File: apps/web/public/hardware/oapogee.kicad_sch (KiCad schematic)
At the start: 37 parts, among them J1 USB-C-16P, J2 S2B-PH-K-S, J3 ANT-902-928, J4 SWD-PADS, SW1 ARM-SWITCH, SW2 BOOT-BUTTON, SW3 RESET-BUTTON, U1 MCP73831, U2 TPS63001, U3 RP2350A, U4 W25Q128JVSIQ, U5 BMP390, U6 ICM-42688-P, U7 ADXL375, U8 SX1262, U9 MAX-M10S

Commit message: Replace the addressable LED, and catch the export lying about it
The status LED is three plain dice in one package now, driven by three pins
through three resistors, rather than an addressable part on one. The reason is
in the bill of materials: the WS2812 family wants a supply above the only rail
this board has, and a part run under its minimum works for whoever tested it and
does something else cold. One resistor per colour because the three dice do not
share a forward voltage, so a single shared one gives three brightnesses and no
way to fix one without moving the others.

Doing it exposed something worse than the LED.

Renaming three pins on the microcontroller left a stale entry in its schematic
pin arrangement, which still named the old label. tscircuit could not resolve
it, and the whole chip failed to create. The export printed success and exited
zero. The netlist came out with 64 of its 123 traces, missing every connection
that touches the microcontroller, and check-pcb reported a clean board: nothing
was unrouted, because the traces that would have been unrouted no longer
existed. I nearly committed a fabrication package for a board with no
microcontroller connected to anything.

Two checks now stand in front of that. Source errors are read before anything
else, because a netlist missing half its connections is not a board with a
routing problem, it is not the board. And the number of traces declared in the
circuit source is compared against the number that reached the netlist, since a
selector that resolves to nothing removes a connection without removing a line
of source, which is invisible to every other measurement. Both are blockers.

The board is 35 components, 119 routed traces, 195 vias, nothing missing,
nothing unconnected, no placement errors, fabrication package regenerated.
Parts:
- removed D1: RGB-LED, symbol Device:U_RGB-LED
- removed GND (x4): GND, symbol Custom:rail_down
- added D1: RGB-LED-CC, symbol Device:U_RGB-LED-CC
- added GND (x3): GND, symbol Custom:rail_down
- added R10: 330Ω, symbol Device:boxresistor_right
- added R11, R12: 220Ω, symbol Device:boxresistor_right
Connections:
- net GND: now also J4.3 (GND), D1.4 (K)
- net at SW1.2 (B): now also LS1.2 (GND); no longer J4.3 (GND)
- net U3_LED renamed U3_LED_R
- net U3_LED_R: now also R10.1
- new net: D1.2 (A_G), R11.2
- new net: D1.1 (A_R), R10.2
- new net D1_A_B: D1.3 (A_B), R12.2
- new net U3_LED_B: R12.1, U3.13 (LED_B)
- new net U3_LED_G: R11.1, U3.16 (LED_G)

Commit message: Choose the remaining parts, and fix what the datasheets said was wrong
The bill of materials had eleven rows with no part behind them, which meant
the design was not actually finished: several of those rows decide how the
board behaves rather than just what it costs. Reading the datasheets to close
them turned up two things the schematic had wrong.

The buck-boost's output capacitor was 10 uF. SLVS520C section 8.2.2.3.2 asks
for a nominal 15 uF, and a small ceramic delivers well under its marked value
under DC bias, so the rail was short of the datasheet twice over. C1 and C2
were one BOM line and are now two, because the datasheet asks for two values:
at least 4.7 uF in, 15 uF nominal out. C2 is 22 uF to leave room for derating.

The status LED was described as common anode in the BOM and wired as common
cathode on the schematic. The schematic was right.

Parts now chosen, each with the datasheet facts that chose them:

  LS1  Murata PKLCS1212E4001-R1, piezo rather than magnetic. A piezo element
       is capacitive, so a pin drives it directly; a magnetic buzzer is a coil
       and would have brought a transistor and a flyback diode with it.
  SW1  C&K JS102011SCQN, SPDT with one throw wired. Driving the spare throw
       would give a defined level in both positions, but the wiper is open
       mid-throw, so the pin would float on every actuation.
  J1   GCT USB4085-GF-A, through hole. The USB connector is the only part of
       a flight computer a person yanks on, and surface mount pads tear off.
  J3   Hirose U.FL-R-SMT-1(10). A socket, because the radiator is still an
       open measurement and soldering it down would close the question by
       making it too annoying to ask. Thirty mating cycles: fit it once.
  SW2  Omron B3U-1000P for boot and reset. 153 gf is stiff on purpose.
  SW3
  L2   Coilcraft LPS3015 or another series from SLVS520C Table 2. At 2.5 MHz
       the core material decides efficiency, so the datasheet's own list is
       the selectio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
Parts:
- removed GND (x3): GND, symbol Custom:rail_down
- removed J1: USB-C-16P, symbol Device:U_USB-C-16P
- removed J3: ANT-902-928, symbol Device:U_ANT-902-928
- removed LS1: PIEZO-BUZZER, symbol Device:U_PIEZO-BUZZER
- removed SW1: ARM-SWITCH, symbol Device:U_ARM-SWITCH
- removed SW2: BOOT-BUTTON, symbol Device:U_BOOT-BUTTON
- removed SW3: RESET-BUTTON, symbol Device:U_RESET-BUTTON
- added GND (x3): GND, symbol Custom:rail_down
- added J1: USB4085-GF-A, symbol Device:U_USB4085-GF-A
- added J3: U.FL-R-SMT-1(10), symbol Device:U_U.FL-R-SMT-1(10)
- added LS1: PKLCS1212E4001-R1, symbol Device:U_PKLCS1212E4001-R1
- added SW1: JS102011SCQN, symbol Device:U_JS102011SCQN
- added SW2, SW3: B3U-1000P, symbol Device:U_B3U-1000P
- C2: value 10uF -> 22uF
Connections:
- net GND: now also J1.2 (GND), SW2.3 (B1), SW2.4 (B2), SW3.3 (B1), SW3.4 (B2)
- net J1_CC2: now also J1.6 (CC2)
- net U3_ARM: now also SW1.1 (A)
- net U3_BUZZER: now also LS1.1 (IN)
- net U3_QSPI_CS: now also SW2.1 (A1), SW2.2 (A2)
- net U3_RUN: now also SW3.2 (A2)
- net U3_USB_DM: now also J1.4 (DM)
- net U3_USB_DP: now also J1.3 (DP)
- net U8_ANT: now also J3.1 (ANT)
- net at U1.4 (VDD): now also J1.1 (VBUS)
- net at R1.1: now also J1.5 (CC1)
- net at U9.2 (GND): now also J3.2 (GND)
- new net: LS1.2 (GND), SW1.2 (B)

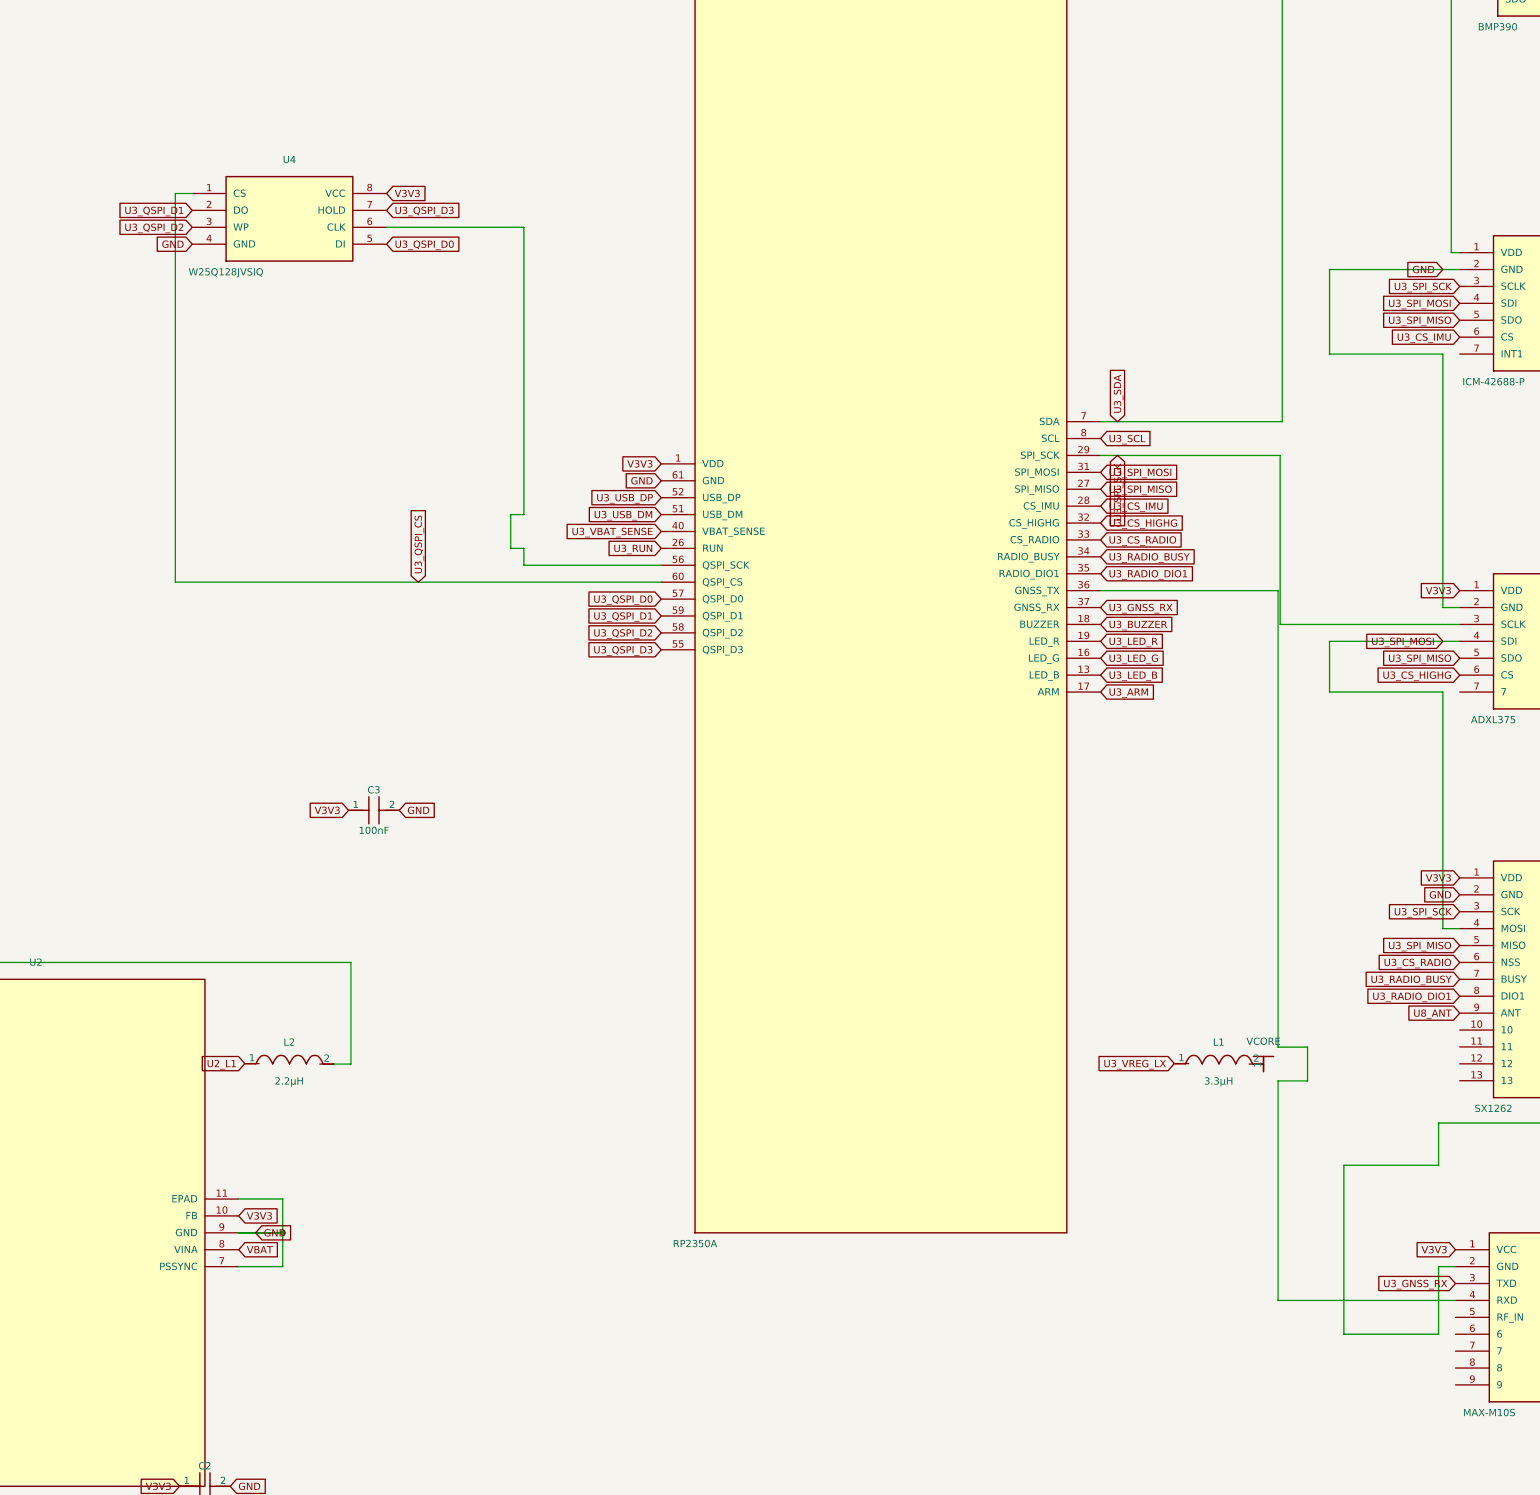
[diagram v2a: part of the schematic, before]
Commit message: Add the crystal, without which the board cannot be flashed
XIN and XOUT were declared on the RP2350 and connected to nothing. That is not
a missing refinement, it is a dead board: "Hardware design with RP2350" chapter
4 says the internal oscillator's frequency is not well defined or controlled,
varying by chip, supply and temperature, and that applications relying on exact
frequencies are not possible without an external source, naming USB as the
example. USB is the only connector this board has and drag-and-drop UF2 loading
is why this microcontroller family was chosen at all.

Every value is Raspberry Pi's. Y1 is the ABM8-272-T3 they specify and the Pico 2
uses. C4 and C5 are 15 pF, which in series is 7.5 pF, plus the 3 pF of track and
pin parasitic capacitance the guide tells you to assume, reaching 10.5 pF
against the crystal's 10 pF load. R13 is the 1k that stops a 50 ohm ESR crystal
being overdriven at 3.3 V IOVDD. The load capacitors are C0G rather than the
X5R used elsewhere, because a payload sits in the sun and then climbs into cold
air, and a load capacitance that drifts detunes the oscillator.

The board is 39 components and 128 routed traces, still with no fabrication
blockers. The build page now solders the crystal as a fact rather than "if the
design uses one", and fits the arming switch, which neither path did.

Also, the ground station page said each packet carries the payload's device
identifier. It does not. The header is eight bytes of version, type, sequence,
state and timestamp, and there is no identifier anywhere in it. The identity
exists but is written to the flight log, so it tells you whose flight it was
afterwards and not at the time. The page now says that, says what to do instead
(agree different frequencies), and the question of whether an identifier belongs
in the header is written up in open-questions with the airtime cost stated
rather than settled quietly.

Checkpoint 8 sent the reader to a stability margin range on the safety page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
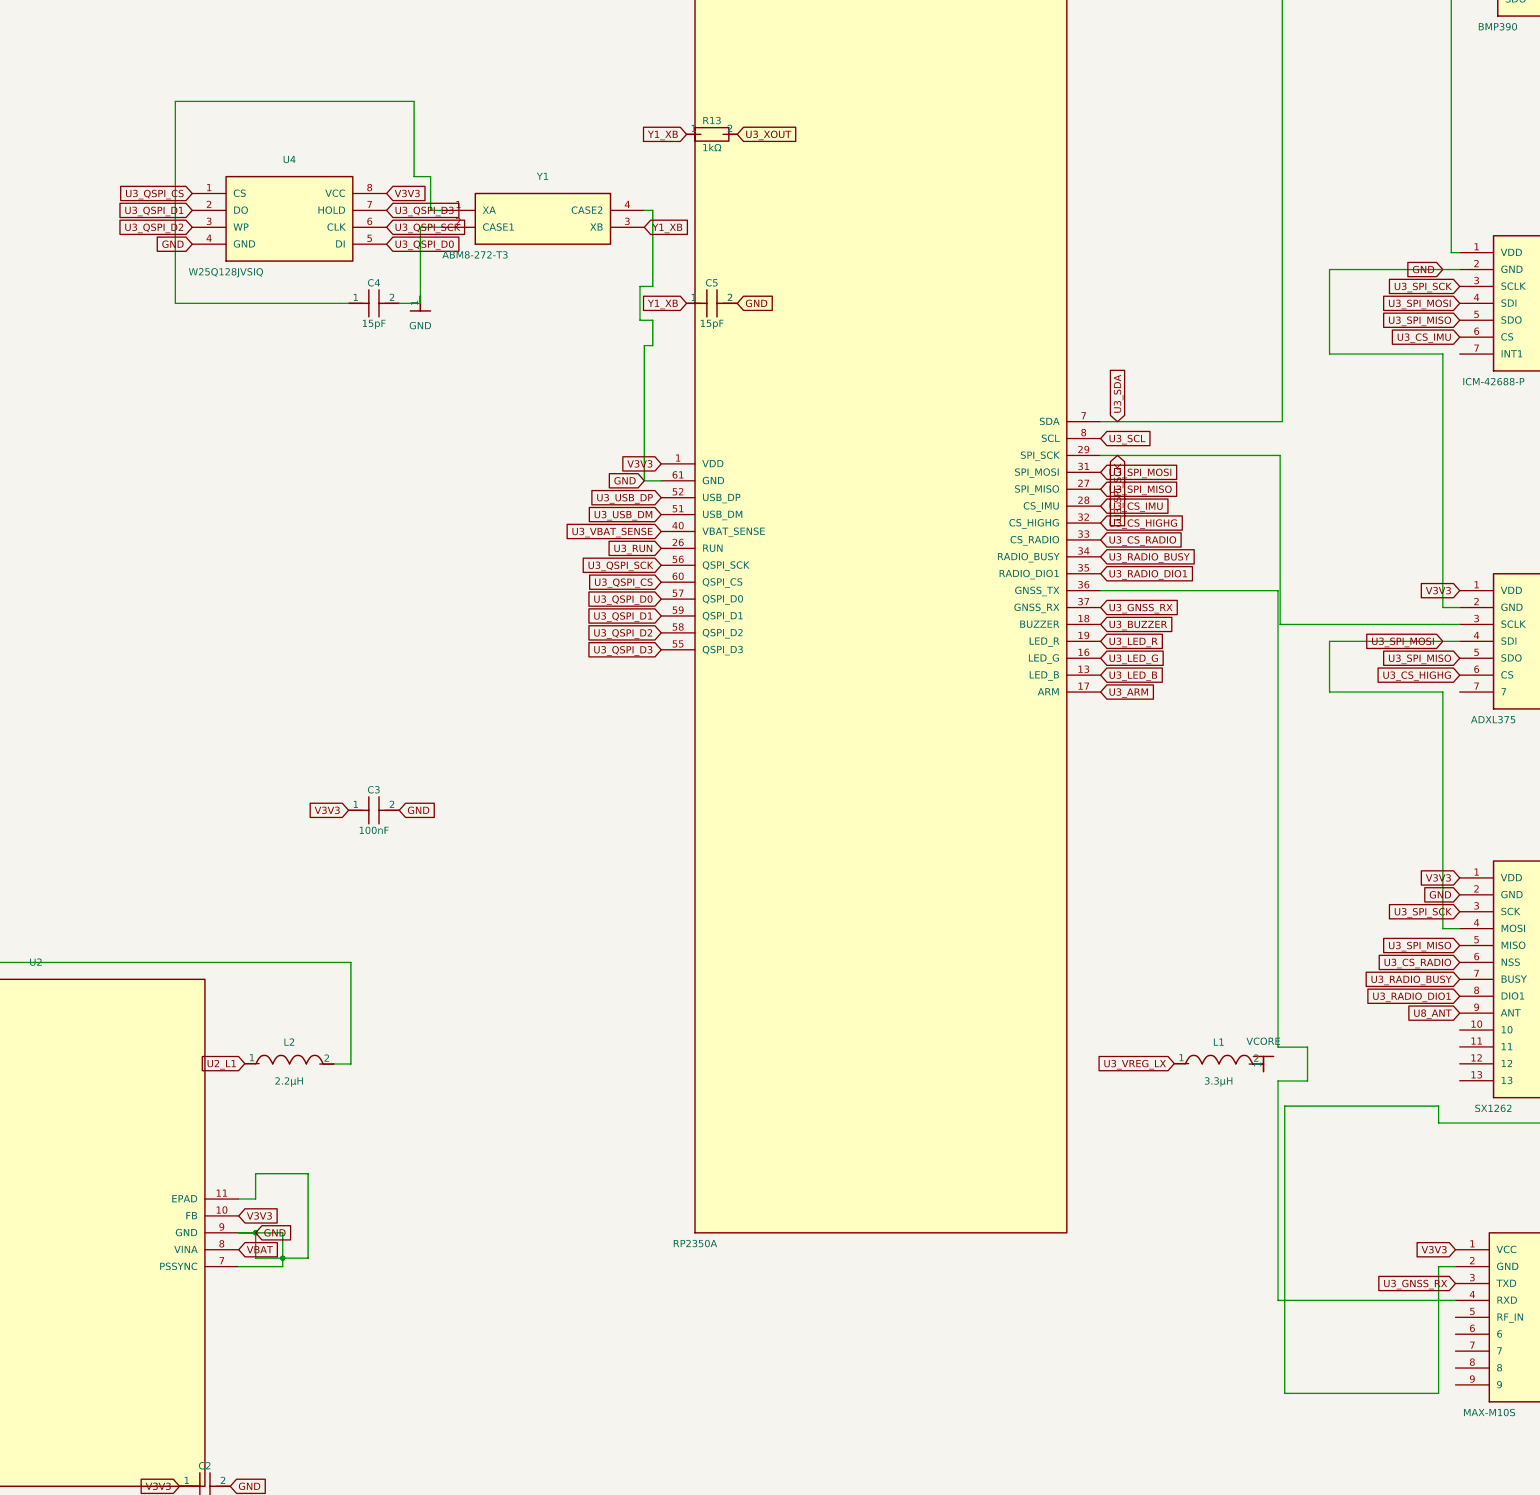
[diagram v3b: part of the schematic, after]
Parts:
- removed GND (x3): GND, symbol Custom:rail_down
- added C4, C5: 15pF, symbol Device:capacitor_right
- added GND (x4): GND, symbol Custom:rail_down
- added R13: 1kΩ, symbol Device:boxresistor_right
- added Y1: ABM8-272-T3, symbol Device:U_ABM8-272-T3
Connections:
- net GND: now also C5.2, Y1.4 (CASE2)
- net U3_QSPI_SCK: now reaches U3.56 (QSPI_SCK), U4.6 (CLK)
- new net: C4.1, Y1.1 (XA)
- new net: C4.2, Y1.2 (CASE1)
- new net U3_XOUT: R13.2
- new net Y1_XB: C5.1, R13.1, Y1.3 (XB)

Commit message: The GNSS receiver had no antenna, and a footprint that did not exist
RF_IN was declared on the receiver and connected to nothing. That is a Track
tier that cannot produce a position, which is the one thing that tier exists
for, and it is the second defect of exactly this shape after the crystal: built
cleanly, routed cleanly, exported a clean Gerber package, passed every check
here. A pin nobody connects looks identical to a pin nobody needed.

Fixing it turned up a third. J5 was given `footprint="ufl"`, which tscircuit
does not have. That is not an error that stops anything: the export logs an
invalid-property message, exits zero, and builds the component with no pads at
all. A part with no pads cannot be routed, so its net silently has no copper.
Worse than a wrong footprint, and the only evidence was one line in a JSON file.
J3 had the same class of problem more quietly, carrying an SMA land pattern for
a u.FL part. Both now use a pattern defined in the source.

Three checks, one per defect, because none of these were found by a check:

  A named pin is connected or listed in INTENTIONALLY_UNCONNECTED with the
  reason. Verified by emptying the list and confirming it names the two pins
  that are deliberately open. It would have caught XIN, XOUT and RF_IN.

  A rejected component property is a blocker rather than a log line.

  The count of copper pairs too close together for the cheaper fabricator is
  ratcheted rather than only printed. It went from 37 to 82 in the commit that
  added these two connectors, and nothing said so, because the ratchet only ever
  watched blockers. A number that lives only in an advisory list can double
  while every check prints a reassuring summary.

The board is 40 components, 132 routed traces, 203 vias, no blockers.

The Mounting page now has an antenna section, which it needed the moment there
were two of them: the radio wants to be away from metal and pointed sideways at
somebody on the ground, the GNSS wants to see sky, and t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
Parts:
- removed GND (x4): GND, symbol Custom:rail_down
- added GND (x3): GND, symbol Custom:rail_down
- added J5: U.FL-R-SMT-1(10), symbol Device:U_U.FL-R-SMT-1(10)
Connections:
- net GND: now also J3.2 (GND), J3.3 (GND2), U9.2 (GND), J5.2 (GND), J5.3 (GND2)
- net U9_RF_IN: now reaches U9.5 (RF_IN)
- net U9_RF_IN: now also J5.1 (SIG)
